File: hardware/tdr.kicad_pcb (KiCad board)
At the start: 4 copper layers, 239 parts, among them J201 Conn_02x01, J202 Conn_Coaxial, J203 Conn_Coaxial, J204 Conn_Coaxial, J205 Conn_Coaxial, J206 Conn_Coaxial, J207 Conn_Coaxial, J208 Conn_Coaxial, J209 Conn_Coaxial, J210 Barrel_Jack_Switch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

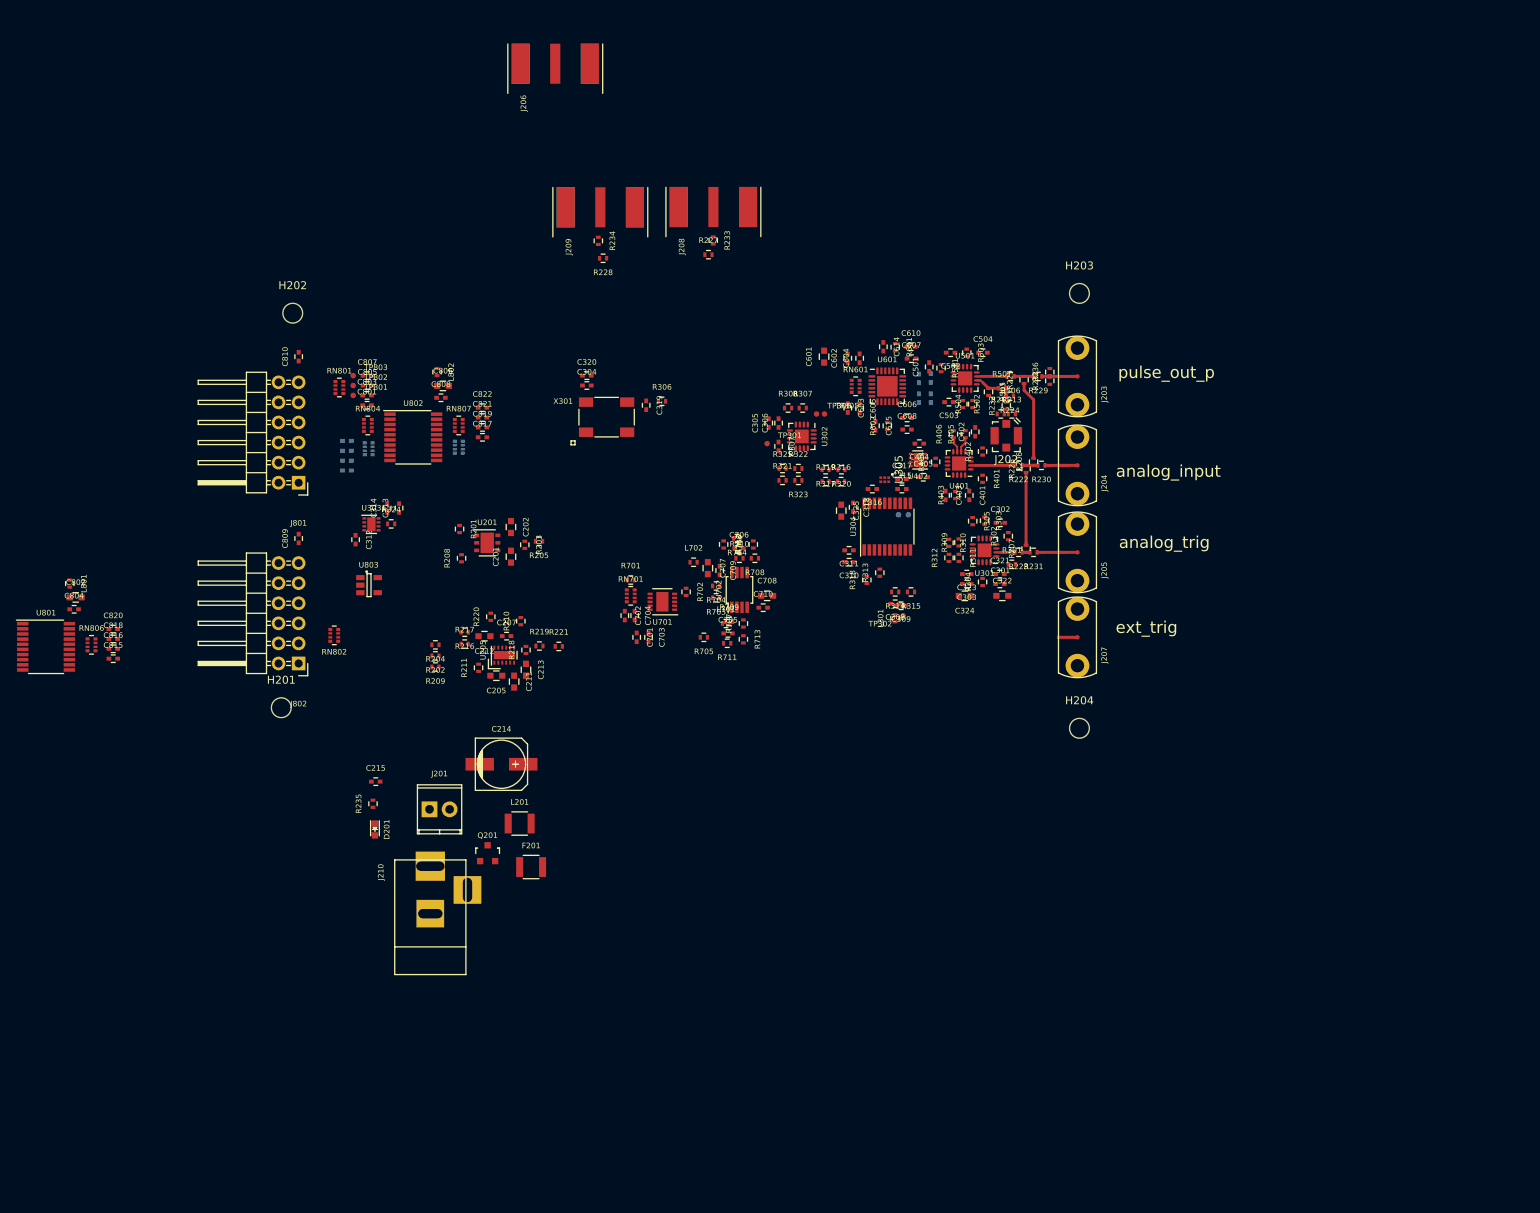
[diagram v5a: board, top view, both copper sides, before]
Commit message: finished first pass component placement and drc setup, swapped digital pins for easier routing
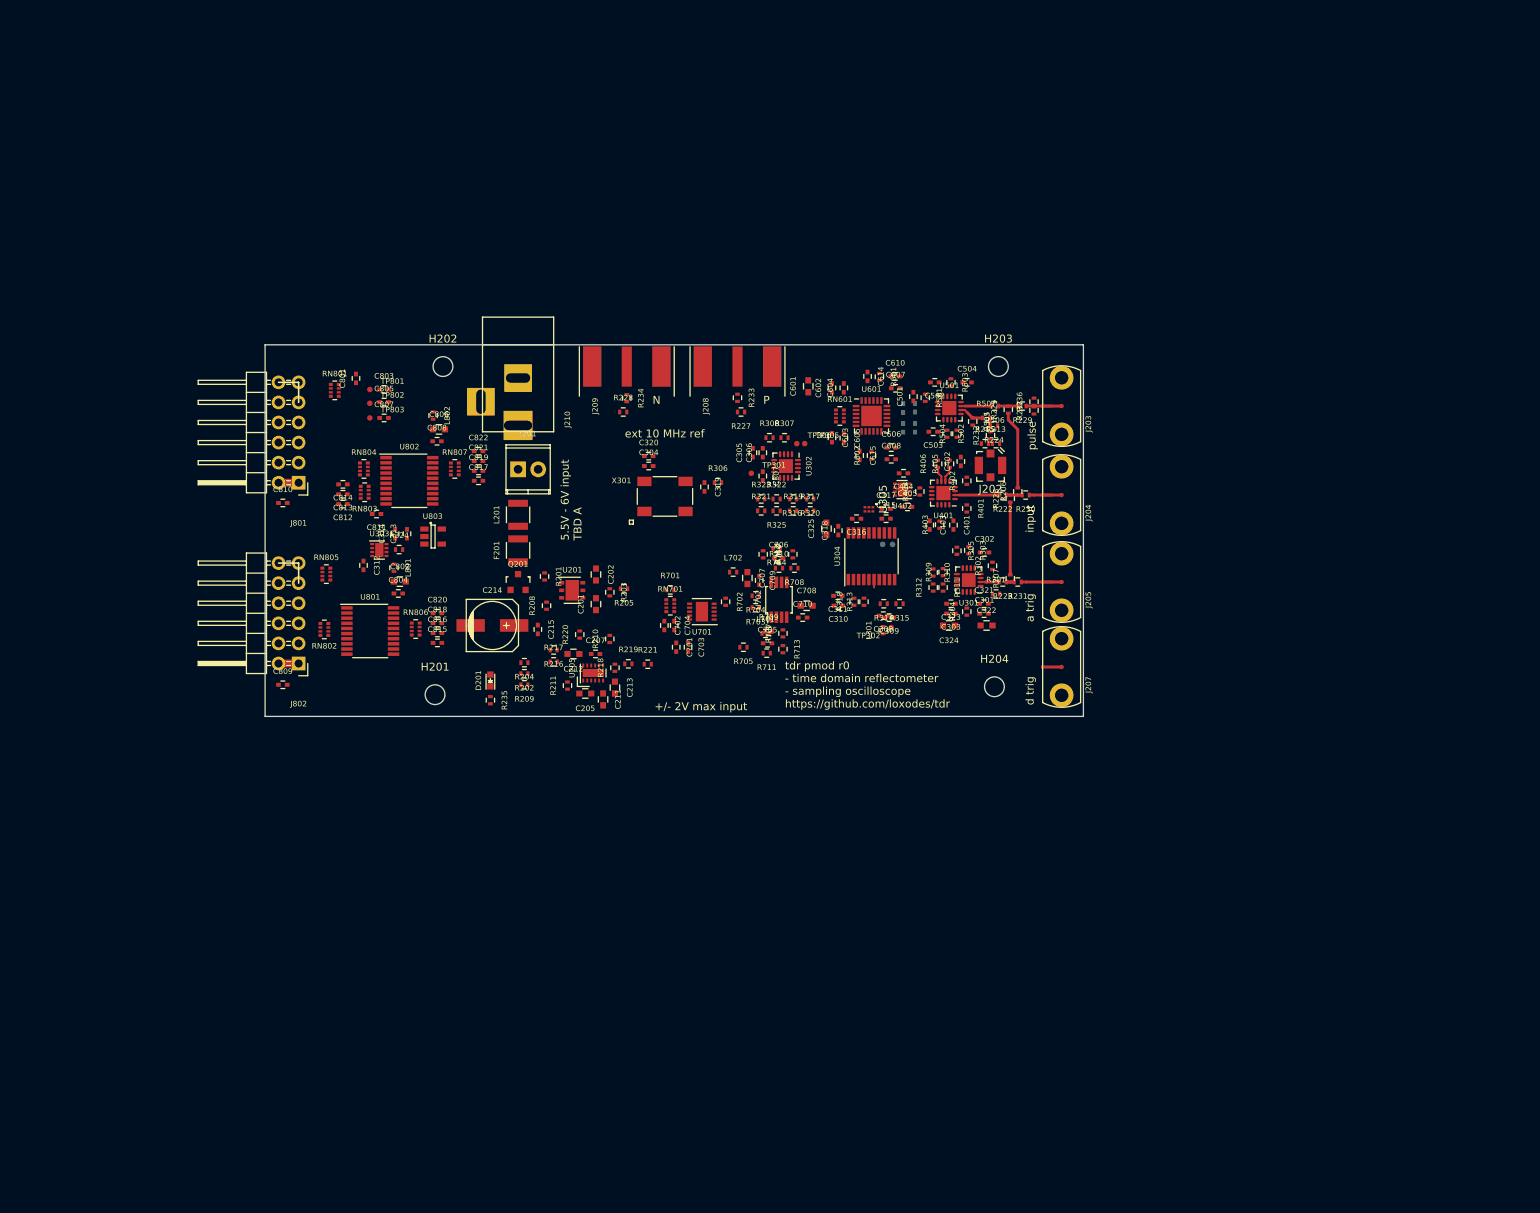
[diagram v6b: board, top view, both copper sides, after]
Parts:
- removed J206: Conn_Coaxial, vna_footprints:732511150_sma_thin
- C809, C810: value C_Small -> 100 nF
- C811, C812, C813, C814, RN803, RN805: moved to F.Cu
- J801, J802: value Conn_02x06_Odd_Even -> Conn_02x06_Counter_Clockwise
- moved J210 69.0 mm to (122.8, 62.5), turned to 270 degrees
- moved J201 44.4 mm to (122.8, 74.2)
- moved C802 41.0 mm to (107.8, 88.5)
- moved C804 41.0 mm to (107.6, 90.0)
- moved C815 41.0 mm to (112.5, 96.2)
- moved C816 41.0 mm to (112.5, 95.0)
- moved C818 41.0 mm to (112.5, 93.7)
- moved C820 41.0 mm to (112.5, 92.5)
- moved L801 41.0 mm to (107.0, 86.7)
- moved RN806 41.0 mm to (109.8, 94.5)
- moved U801 41.0 mm to (104.0, 94.7)
- moved F201 40.1 mm to (122.8, 84.5), turned to 90 degrees
- moved L201 39.1 mm to (122.8, 80.0), turned to 90 degrees
- moved Q201 34.5 mm to (122.8, 88.5)
- moved C215 28.1 mm to (125.2, 94.5), turned to 270 degrees
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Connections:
- J801 pad 1: Net-(J801-Pad1) -> +3.3VP
- J801 pad 10: GND -> Net-(J801-Pad10)
- J801 pad 11: +3.3VP -> Net-(J801-Pad11)
- J801 pad 12: +3.3VP -> Net-(J801-Pad12)
- J801 pad 2: Net-(J801-Pad2) -> +3.3VP
- J801 pad 3: Net-(J801-Pad3) -> GND
- J801 pad 4: Net-(J801-Pad4) -> GND
- J801 pad 9: GND -> Net-(J801-Pad9)
- J802 pad 1: Net-(J802-Pad1) -> +3.3VP
- J802 pad 10: GND -> Net-(J802-Pad10)
- J802 pad 11: +3.3VP -> Net-(J802-Pad11)
- J802 pad 12: +3.3VP -> Net-(J802-Pad12)
- J802 pad 2: Net-(J802-Pad2) -> +3.3VP
- J802 pad 3: Net-(J802-Pad3) -> GND
- J802 pad 4: Net-(J802-Pad4) -> GND
- J802 pad 5: Net-(J802-Pad5) -> /fpga_connector/EXT_COMP_OUT
- J802 pad 9: GND -> Net-(J802-Pad9)
- RN801 pad 1: Net-(J801-Pad7) -> Net-(J801-Pad12)
- RN801 pad 2: Net-(J801-Pad5) -> Net-(J801-Pad11)
- RN801 pad 3: Net-(J801-Pad3) -> Net-(J801-Pad10)
- RN801 pad 4: Net-(J801-Pad1) -> Net-(J801-Pad9)
- RN801 pad 5: /clock/CLK_FPGA -> Net-(C807-Pad1)
- RN801 pad 6: Net-(C803-Pad1) -> Net-(C805-Pad1)
- RN801 pad 7: Net-(C805-Pad1) -> Net-(C803-Pad1)
- RN801 pad 8: Net-(C807-Pad1) -> /clock/CLK_FPGA
- RN802 pad 1: /fpga_connector/EXT_COMP_OUT -> /fpga_connector/EXT_DELAY_SCK
- RN802 pad 2: /fpga_connector/EXT_DELAY_SDIN -> /fpga_connector/EXT_DELAY_~EN
- RN802 pad 3: /fpga_connector/EXT_DELAY_~EN -> /fpga_connector/EXT_DELAY_SDIN
- RN802 pad 4: /fpga_connector/EXT_DELAY_SCK -> (no net)
- RN802 pad 5: Net-(J802-Pad7) -> (no net)
- RN802 pad 6: Net-(J802-Pad5) -> Net-(J802-Pad8)
- RN802 pad 7: Net-(J802-Pad3) -> Net-(J802-Pad7)
- RN802 pad 8: Net-(J802-Pad1) -> Net-(J802-Pad6)
- RN803 pad 5: /fpga_connector/DELAY_SLOAD -> /fpga_connector/SEL1
- RN803 pad 6: /clock/CLK_SEL -> /fpga_connector/SEL0
- RN803 pad 7: /fpga_connector/SEL0 -> /clock/CLK_SEL
- RN803 pad 8: /fpga_connector/SEL1 -> /fpga_connector/DELAY_SLOAD
- RN804 pad 1: Net-(J801-Pad2) -> Net-(J801-Pad8)
- RN804 pad 2: Net-(J801-Pad4) -> Net-(J801-Pad7)
- RN804 pad 4: Net-(J801-Pad8) -> Net-(J801-Pad5)
- RN805 pad 1: Net-(J802-Pad2) -> Net-(J802-Pad12)
- RN805 pad 2: Net-(J802-Pad4) -> Net-(J802-Pad11)
- RN805 pad 3: Net-(J802-Pad6) -> Net-(J802-Pad10)
- RN805 pad 4: Net-(J802-Pad8) -> Net-(J802-Pad9)
- U802 pad 3: Net-(RN803-Pad1) -> Net-(RN803-Pad4)
- U802 pad 5: Net-(RN803-Pad2) -> Net-(RN803-Pad3)
- U802 pad 7: Net-(RN803-Pad3) -> Net-(RN803-Pad2)
- U802 pad 9: Net-(RN803-Pad4) -> Net-(RN803-Pad1)
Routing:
- net +3.3VP: track 0.00 -> 5.08 mm
- net /EXT_TRIG: track 0.00 -> 0.98 mm
- added copper zone on In1.Cu, net GND
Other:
- board outline added: 103.5 x 47 mm
- net class Default: via_dia 0.8 -> 0.51; via_drill 0.4 -> 0.3
- rule trace_min: 0.2 -> 0.127
- rule via_min_drill: 0.3 -> 0.254
- rule via_min_size: 0.4 -> 0.46
- board text added: "+/- 2V max input"
- board text added: "5.5V - 6V input TBD A"
- board text added: "N"
- board text added: "P"
- board text added: "a trig"
- board text added: "d trig"
- board text added: "ext 10 MHz ref"
- board text added: "input"
- board text added: "pulse"
- board text added: "tdr pmod r0 - time domain reflectometer - sampling oscilloscope https://github.com/loxodes/tdr"
- board text removed: "analog_input"
- board text removed: "analog_trig"
- board text removed: "ext_trig"
- board text removed: "pulse_out_p"

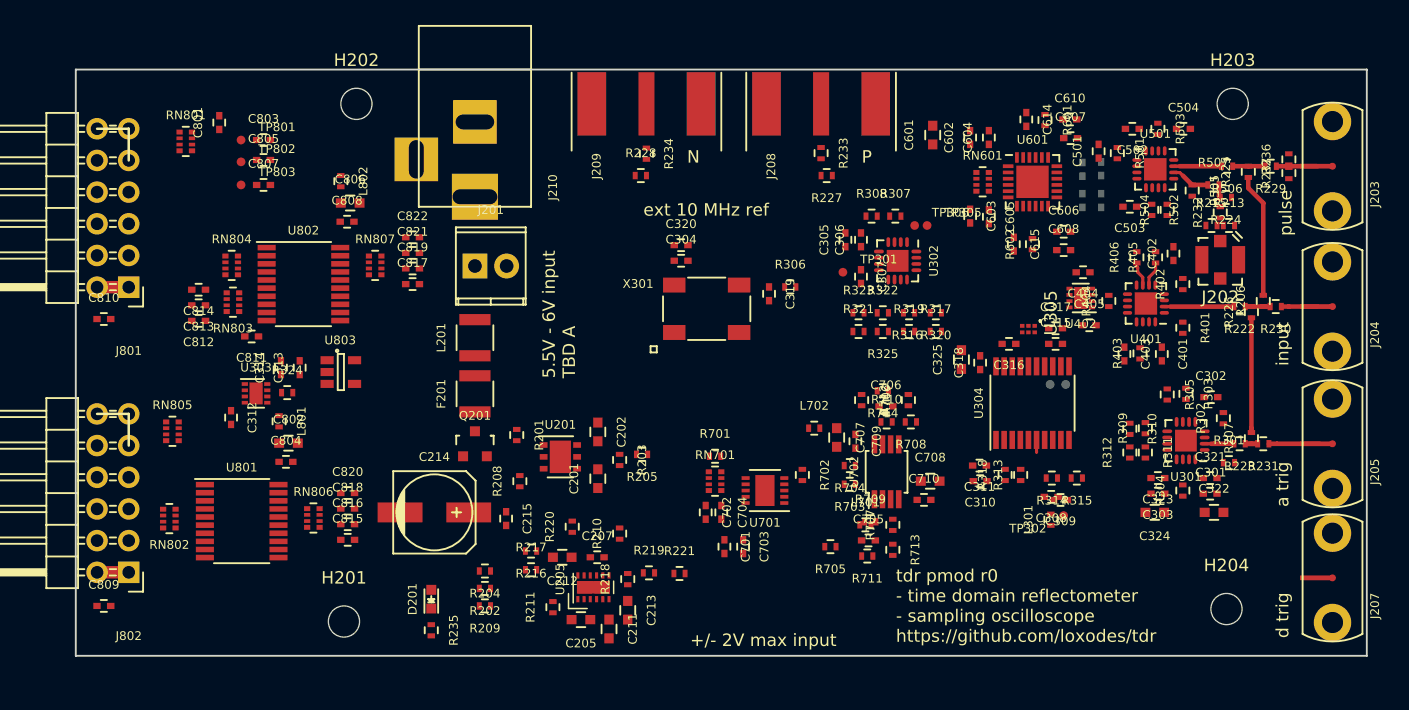
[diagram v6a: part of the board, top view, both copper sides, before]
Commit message: layout of low speed digital traces
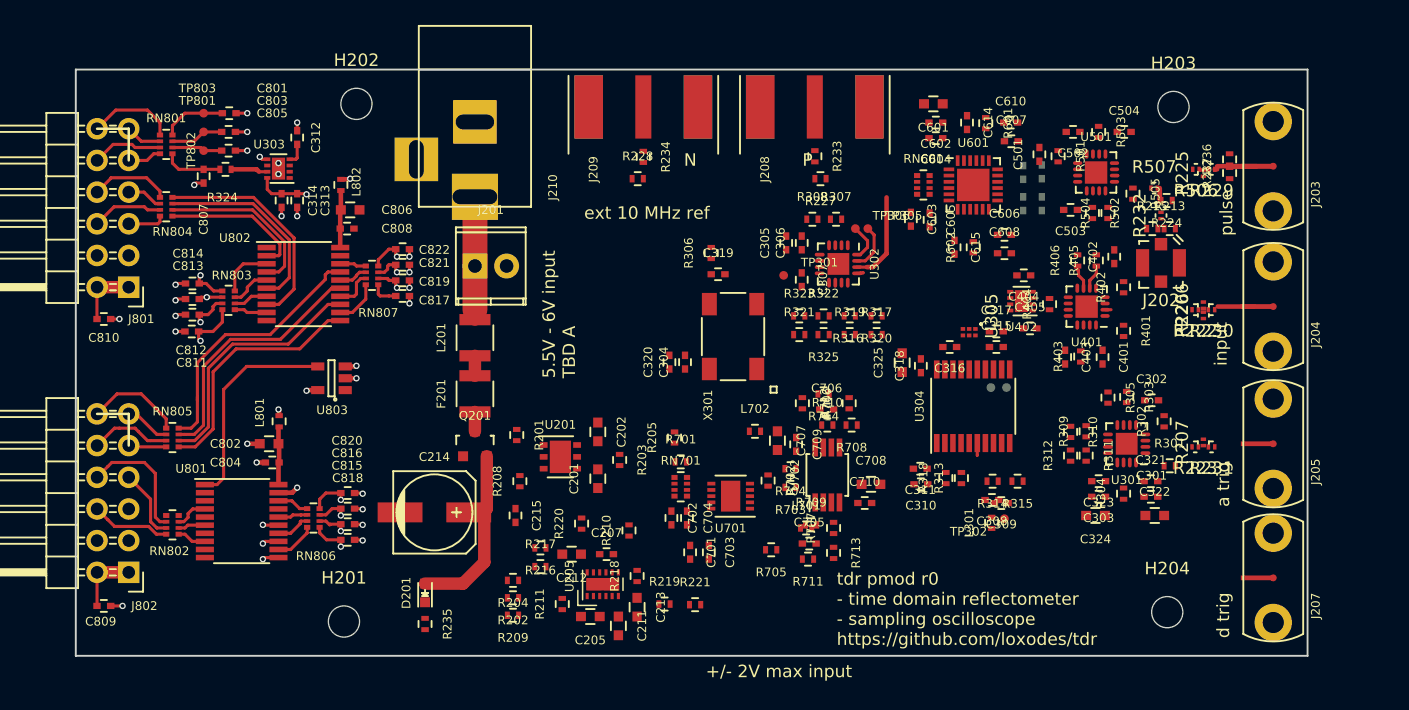
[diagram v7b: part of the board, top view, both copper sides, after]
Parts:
- C801: value 10 pF -> 33 pF
- C807: value 33 pF -> 10 pF
- R206, R207, R222, R223, R225, R226, R229, R230, R231, R232, R506, R507: footprint Resistors_SMD:R_0402 -> Resistors_SMD:R_0201
- moved C312 23.1 mm to (108.5, 64.0), turned to 90 degrees
- moved R324 18.6 mm to (102.8, 66.5), turned to 180 degrees
- moved U303 18.1 mm to (107.0, 66.4), turned to 180 degrees
- moved C313 13.4 mm to (108.5, 69.0), turned to 270 degrees
- moved C314 13.4 mm to (107.2, 69.0), turned to 270 degrees
- moved C320 9.43 mm to (138.3, 82.0), turned to 90 degrees
- moved C304 8.14 mm to (139.6, 82.0), turned to 90 degrees
- moved RN804 7.05 mm to (98.0, 69.5)
- moved R306 6.90 mm to (141.7, 73.2), turned to 90 degrees
- moved TP803 6.49 mm to (101.0, 62.0)
- moved R230 5.16 mm to (181.8, 77.8)
- moved C807 4.85 mm to (101.0, 67.0), turned to 270 degrees
- moved C811 4.82 mm to (100.0, 79.5)
- moved R206 4.81 mm to (181.2, 77.4)
- moved C301 4.76 mm to (176.9, 92.8)
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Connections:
- C801 pad 1: /clock/CLK_FPGA -> Net-(C801-Pad1)
- C807 pad 1: Net-(C807-Pad1) -> /clock/CLK_FPGA
- RN801 pad 5: Net-(C807-Pad1) -> /clock/CLK_FPGA
- RN801 pad 8: /clock/CLK_FPGA -> Net-(C801-Pad1)
- TP803 pad 1: Net-(C807-Pad1) -> Net-(C801-Pad1)
- U802 pad 2: Net-(RN804-Pad8) -> Net-(RN804-Pad5)
- U802 pad 4: Net-(RN804-Pad7) -> Net-(RN804-Pad6)
- U802 pad 6: Net-(RN804-Pad6) -> Net-(RN804-Pad7)
- U802 pad 8: Net-(RN804-Pad5) -> Net-(RN804-Pad8)
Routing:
- net GND: track 0.00 -> 22.9 mm, vias 0 -> 30
- net Net-(RN805-Pad8): track 0.00 -> 21.4 mm
- net Net-(RN805-Pad7): track 0.00 -> 20.6 mm
- net Net-(RN805-Pad6): track 0.00 -> 20.2 mm
- net Net-(RN805-Pad5): track 0.00 -> 19.8 mm
- net Net-(RN804-Pad8): track 0.00 -> 17.9 mm
- net Net-(U801-Pad1): track 0.00 -> 17.1 mm
- net Net-(RN804-Pad7): track 0.00 -> 15.8 mm
- net VPP: track 0.00 -> 15.2 mm
- net Net-(RN804-Pad6): track 0.00 -> 13.6 mm
- net Net-(RN804-Pad5): track 0.00 -> 11.5 mm
- net Net-(J802-Pad8): track 0.00 -> 10.1 mm
- net Net-(R206-Pad2): track 9.95 -> 0.00 mm
- net Net-(J201-Pad1): track 0.00 -> 9.85 mm
- net Net-(R207-Pad2): track 9.20 -> 0.00 mm
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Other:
- board size 103.5 x 47 mm -> 98.8 x 47 mm
- net class Default: clearance 0.2 -> 0.13
- rule trace_clearance: 0.2 -> 0.13
